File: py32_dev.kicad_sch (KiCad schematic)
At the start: 34 parts, among them J1 Board Pwr, J2 Conn_01x18, J3 Conn_01x18, SW1 Usr, SW2 Reset, U1 uA7805, U2 PY32F030K1xT, Y1 24MHz, Y2 32.768KHz

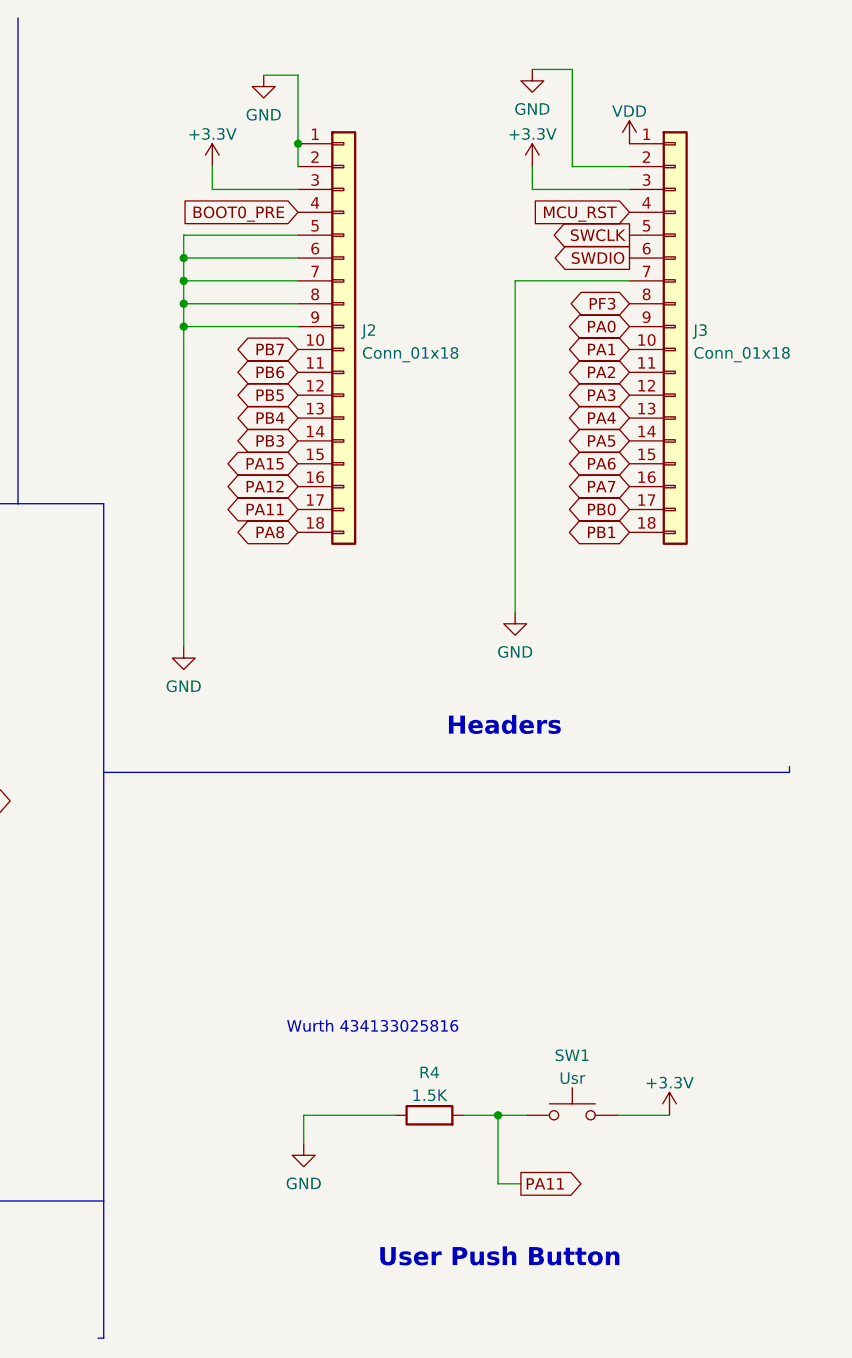
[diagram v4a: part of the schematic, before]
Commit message: Removed R4, user PB swap, back to rev A config
Added link in README to blink firmware repository and puya32 tech docs
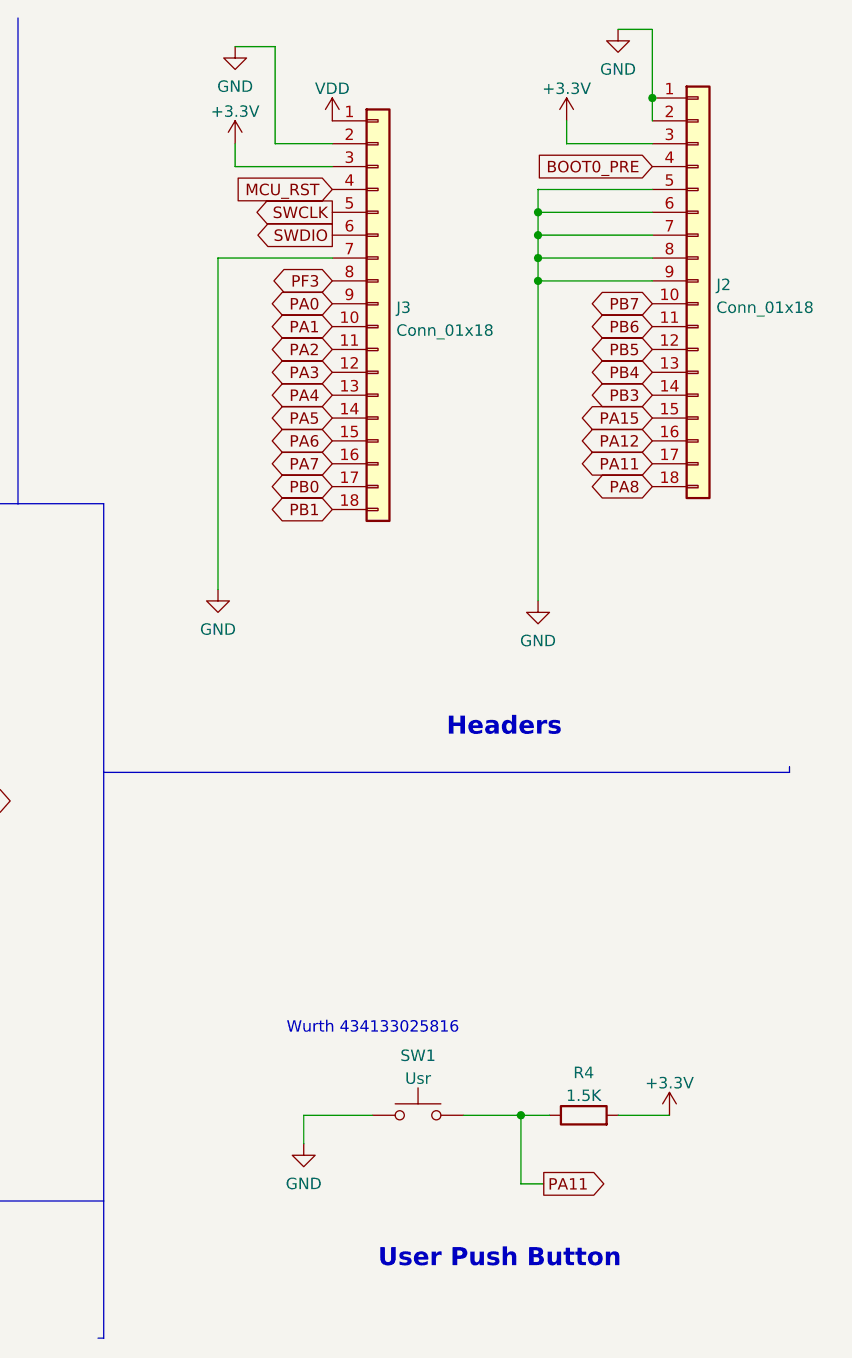
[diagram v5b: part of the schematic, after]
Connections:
- net +3.3V: now also R4.2; no longer SW1.2
- net GND: now also SW1.1; no longer R4.1
- net PA11: now also R4.1, SW1.2; no longer R4.2, SW1.1
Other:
- moved on the sheet: J2, J3, R4, SW1
